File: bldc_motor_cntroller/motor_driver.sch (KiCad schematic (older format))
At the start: 70 parts, among them J10 MR30PW-M 15A (30A), Q3 CSD18540Q5B, Q4 CSD18540Q5B, Q5 CSD18540Q5B, Q6 CSD18540Q5B, Q7 CSD18540Q5B, Q8 CSD18540Q5B, U4 DRV8301DCAR

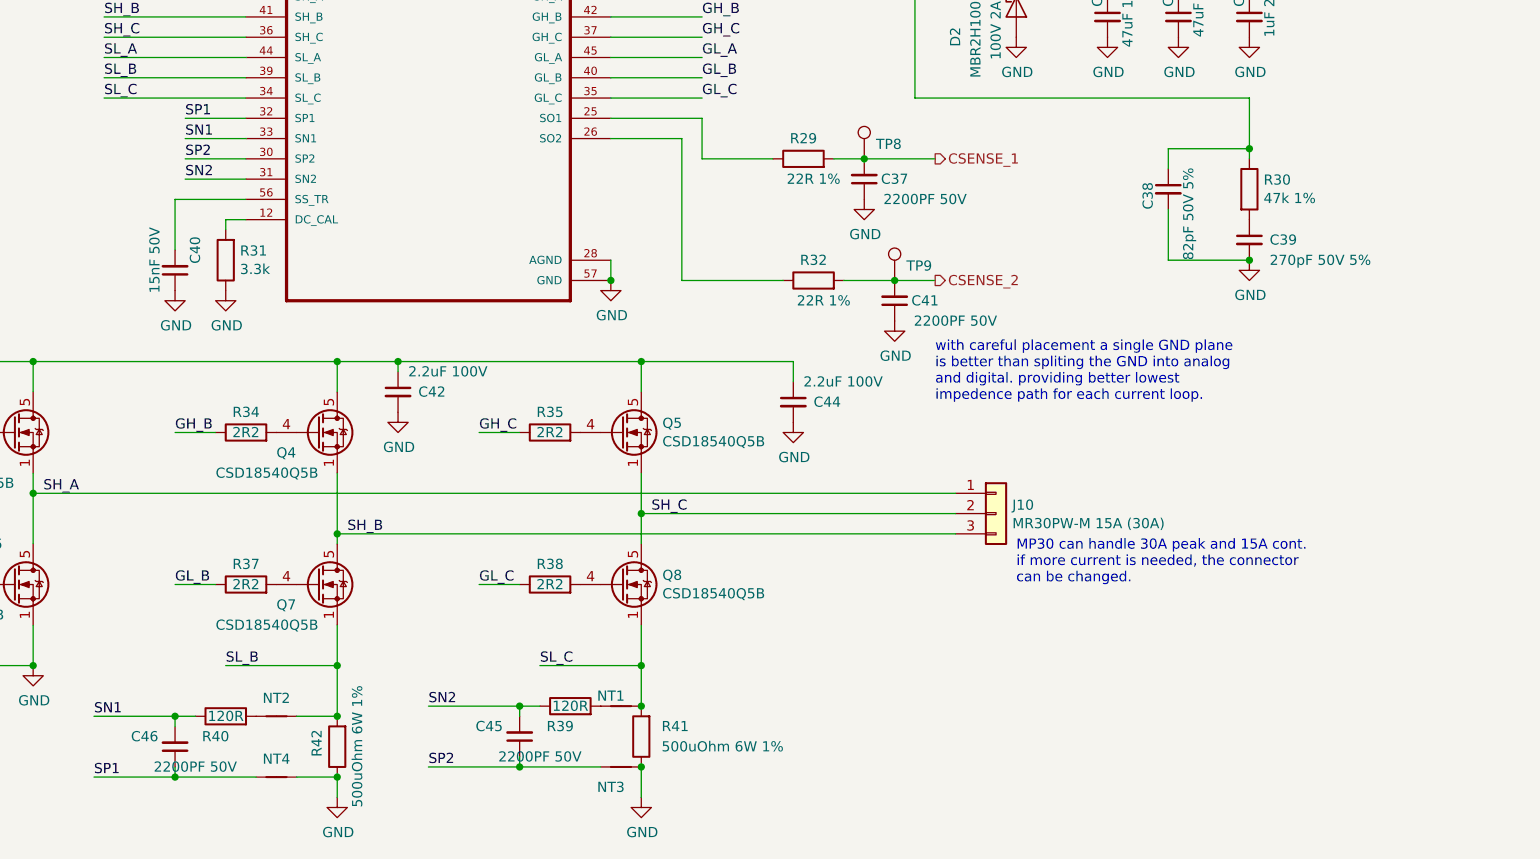
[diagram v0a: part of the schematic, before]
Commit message: improved assembly documentation
Signed-off-by: azmat bilal <azmat.bilal@outlook.com>
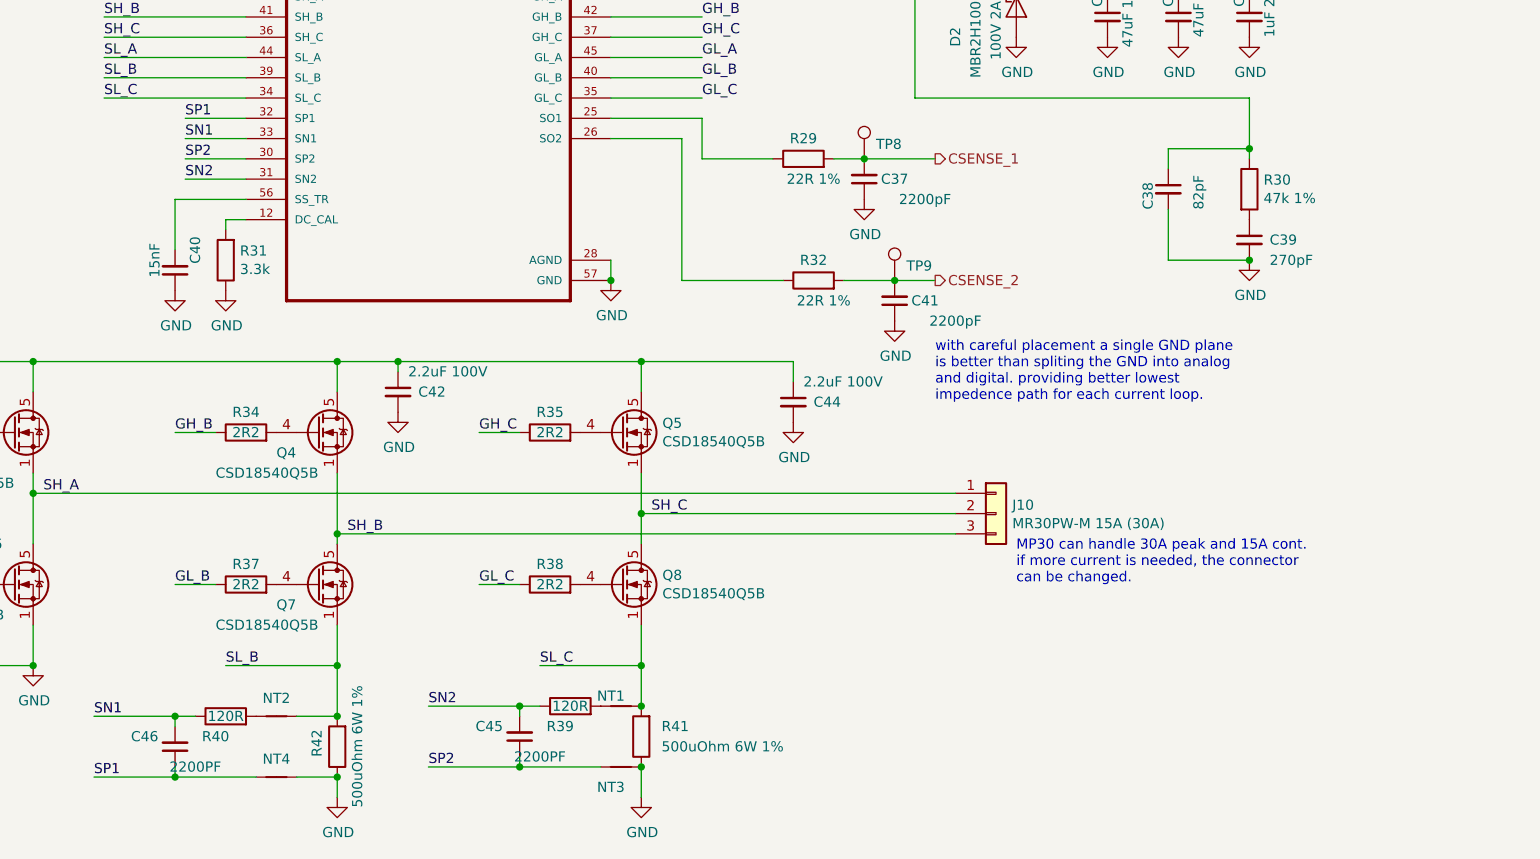
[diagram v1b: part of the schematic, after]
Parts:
- C37, C41: value 2200PF 50V -> 2200pF
- C38: value 82pF 50V 5% -> 82pF
- C39: value 270pF 50V 5% -> 270pF
- C40: value 15nF 50V -> 15nF
- C45, C46: value 2200PF 50V -> 2200PF
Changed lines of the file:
@@
 P 8100 4500
 F 0 "C38" V 8000 4400 50  0000 L CNN
-F 1 "82pF 50V 5%" V 8200 4150 50  0000 L CNN
+F 1 "82pF" V 8250 4400 50  0000 L CNN
 F 2 "Capacitor_SMD:C_0402_1005Metric" H 8100 4500 50  0001 C CNN
 F 3 "~" H 8100 4500 50  0001 C CNN
@@
 P 8500 4750
 F 0 "C39" H 8600 4750 50  0000 L CNN
-F 1 "270pF 50V 5%" H 8600 4650 50  0000 L CNN
+F 1 "270pF" H 8600 4650 50  0000 L CNN
 F 2 "Capacitor_SMD:C_0402_1005Metric" H 8500 4750 50  0001 C CNN
 F 3 "~" H 8500 4750 50  0001 C CNN
@@
 P 3200 7250
 F 0 "C46" H 3350 7200 50  0000 C CNN
-F 1 "2200PF 50V" H 3100 7350 50  0000 C CNN
+F 1 "2200PF" H 3100 7350 50  0000 C CNN
 F 2 "Capacitor_SMD:C_0402_1005Metric" H 3200 7250 50  0001 C CNN
 F 3 "~" H 3200 7250 50  0001 C CNN
@@
 P 4900 7200
 F 0 "C45" H 5050 7150 50  0000 C CNN
-F 1 "2200PF 50V" H 4800 7300 50  0000 C CNN
+F 1 "2200PF" H 4800 7300 50  0000 C CNN
 F 2 "Capacitor_SMD:C_0402_1005Metric" H 4900 7200 50  0001 C CNN
 F 3 "~" H 4900 7200 50  0001 C CNN
@@
 P 3200 4900
 F 0 "C40" V 3100 4800 50  0000 C CNN
-F 1 "15nF 50V" V 3300 4850 50  0000 C CNN
+F 1 "15nF" V 3300 4850 50  0000 C CNN
 F 2 "Capacitor_SMD:C_0402_1005Metric" H 3200 4900 50  0001 C CNN
 F 3 "~" H 3200 4900 50  0001 C CNN
@@
 P 6750 5050
 F 0 "C41" H 6600 5050 50  0000 C CNN
-F 1 "2200PF 50V" H 6450 5150 50  0000 C CNN
+F 1 "2200pF" H 6450 5150 50  0000 C CNN
 F 2 "Capacitor_SMD:C_0402_1005Metric" H 6750 5050 50  0001 C CNN
 F 3 "~" H 6750 5050 50  0001 C CNN
@@
 P 6600 4450
 F 0 "C37" H 6450 4450 50  0000 C CNN
-F 1 "2200PF 50V" H 6300 4550 50  0000 C CNN
+F 1 "2200pF" H 6300 4550 50  0000 C CNN
 F 2 "Capacitor_SMD:C_0402_1005Metric" H 6600 4450 50  0001 C CNN
 F 3 "~" H 6600 4450 50  0001 C CNN

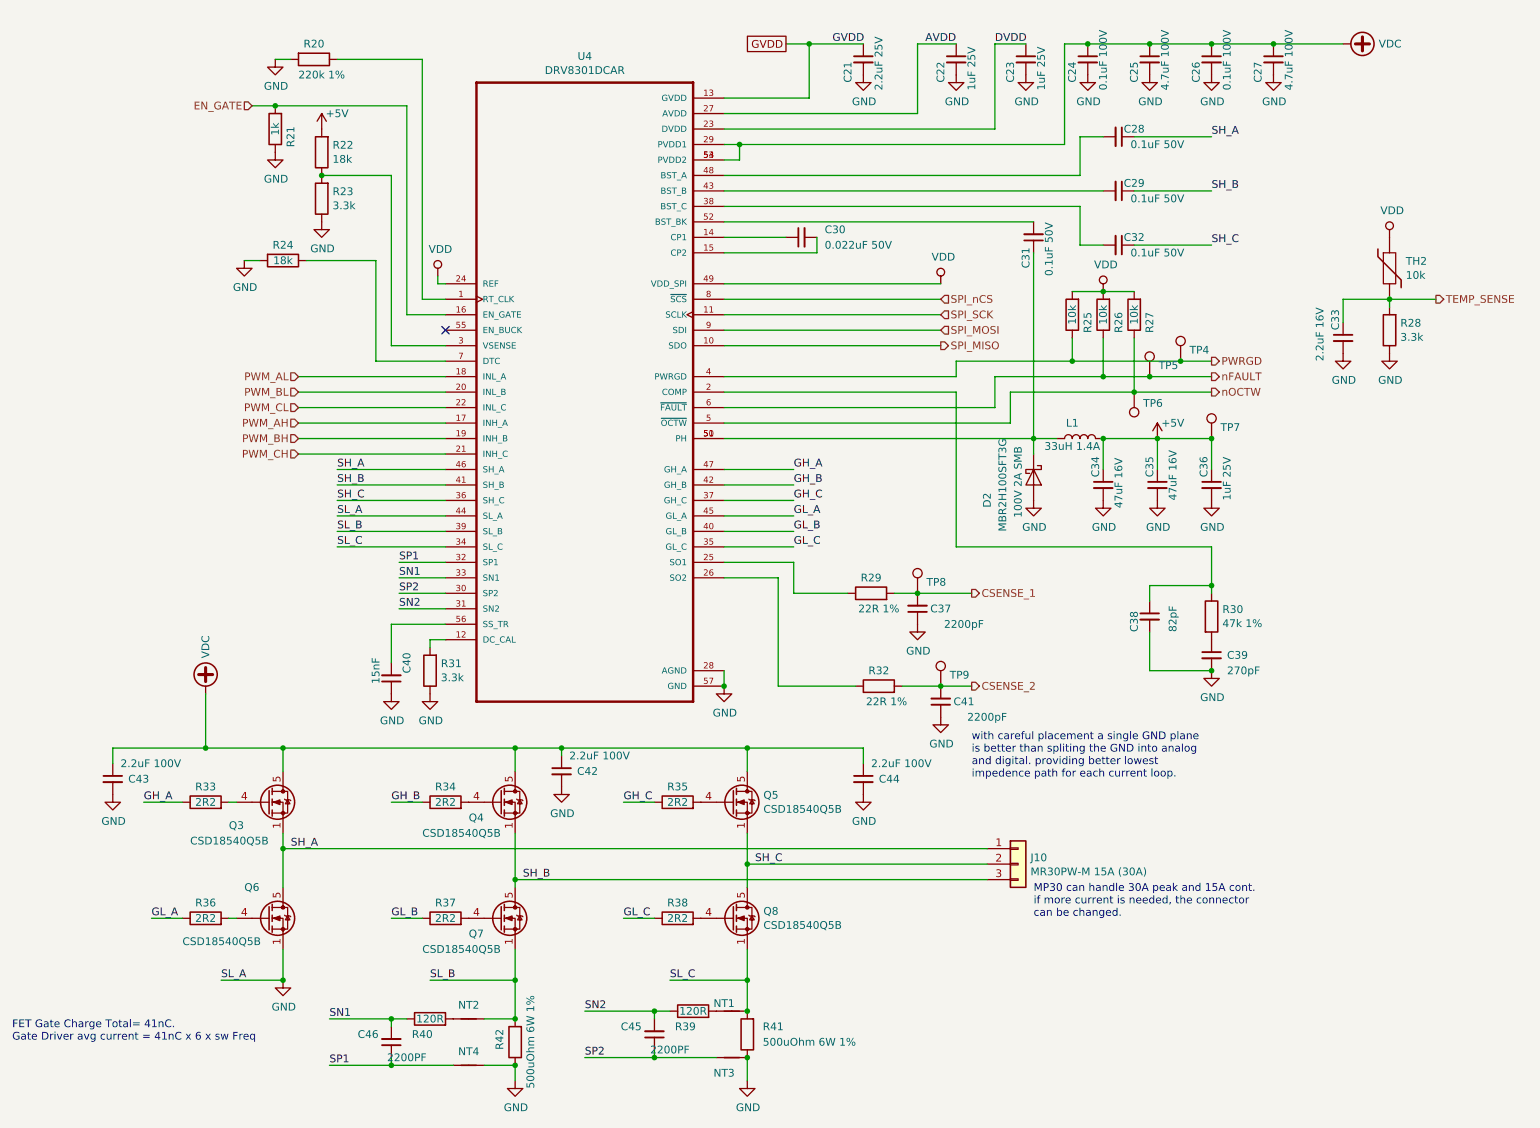
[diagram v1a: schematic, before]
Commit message: improved BOM
Signed-off-by: azmat bilal <azmat.bilal@outlook.com>
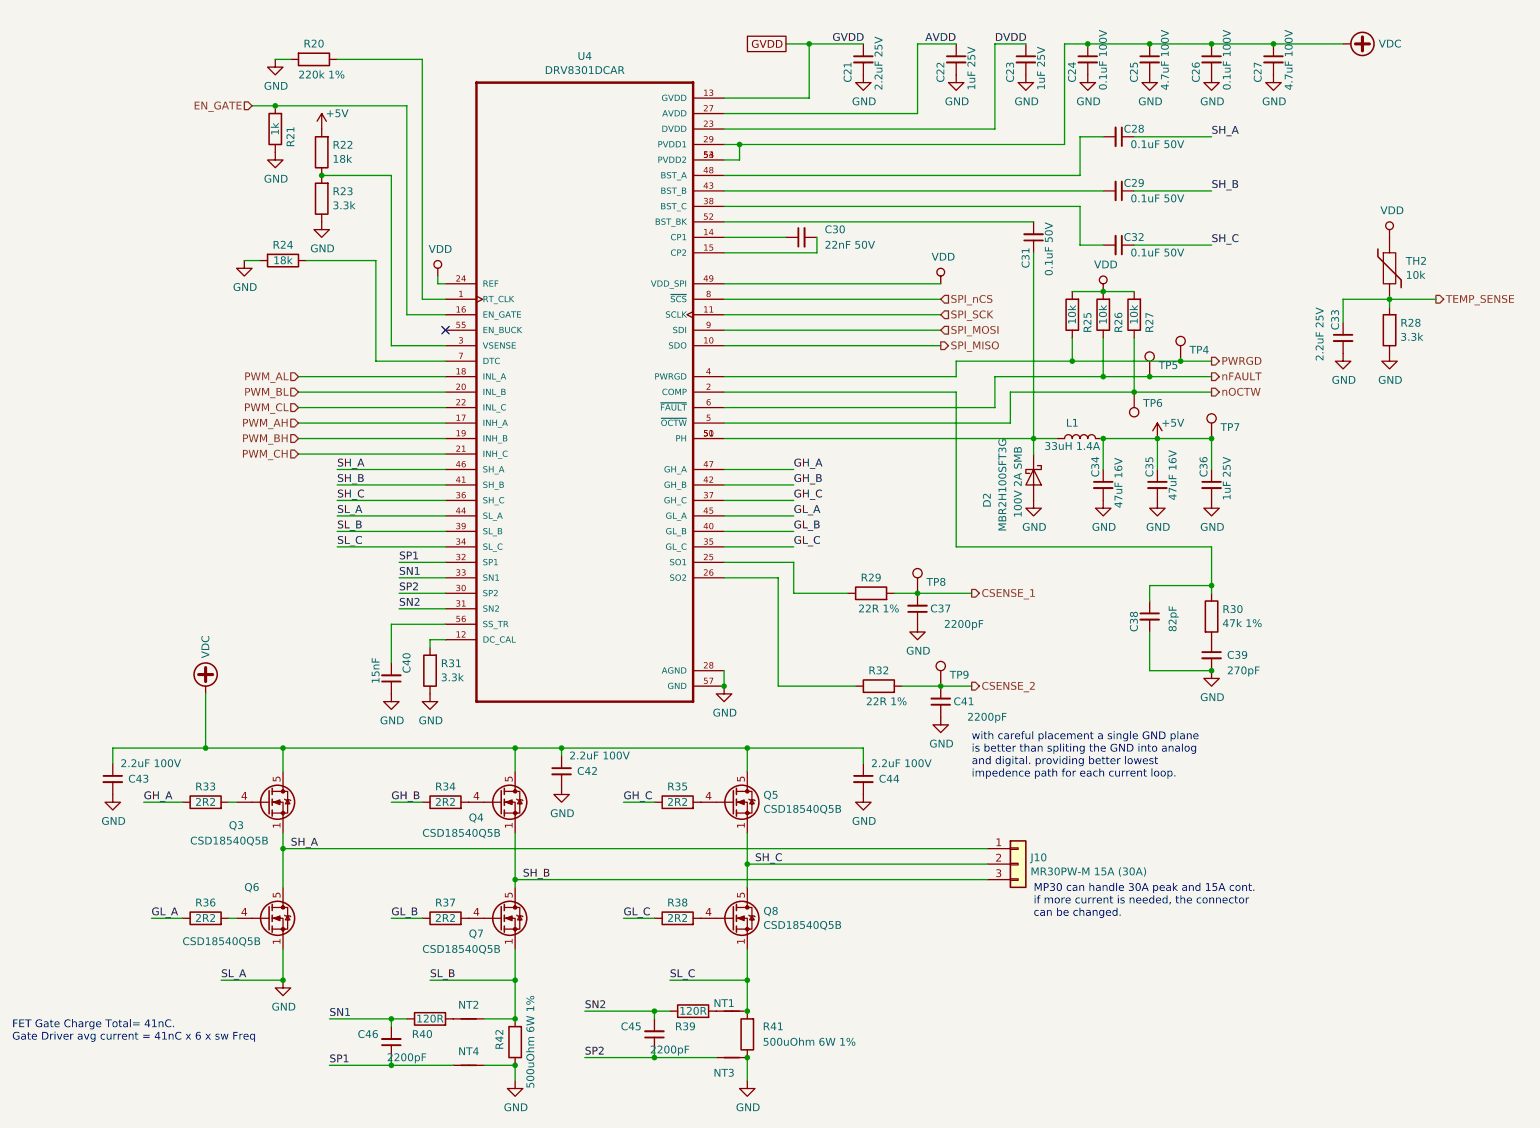
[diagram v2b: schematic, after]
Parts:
- C21: MPN (none) -> GRM155C81E225KE11D
- C22, C23, C36: MPN (none) -> GMK105CC6105MV-F
- C24, C26: MPN (none) -> GRM155R62A104KE14D
- C25, C27: MPN (none) -> HMK325C7475KN-TE
- C28, C29, C31, C32: MPN (none) -> GCM155L8EH104KE07D
- C30: value 0.022uF 50V -> 22nF 50V; MPN (none) -> C0402C223K5REC7411
- C33: value 2.2uF 16V -> 2.2uF 25V; MPN (none) -> GRM155C81E225KE11D
- C34, C35: MPN (none) -> GRM32EC81C476KE15L
- C37, C41: MPN (none) -> C0402C222J3GEC7411
- C38: MPN (none) -> VJ0402A820JXACW1BC
- C39: MPN (none) -> GRM1555C1H271FA01D
- C40: MPN (none) -> GCM155R71E153JA55D
- C42, C43, C44: MPN (none) -> C1210C225K1RACAUTO
- C45, C46: value 2200PF -> 2200pF; MPN (none) -> C0402C222J3GEC7411
- J10, NT1, NT2, NT3, NT4, TP4, TP5, TP6, TP7, TP8, TP9: MPN (none) -> -
- Q3, Q4, Q5, Q6, Q7, Q8: MPN (none) -> CSD18540Q5BT
- R20: MPN (none) -> CRCW0402220KFKEDC
- R21: MPN (none) -> ERJ-2RKF1001X
- R22, R24: MPN (none) -> CRCW040218K0FKED
- R23, R28, R31: MPN (none) -> CRCW04023K30FKEDC
- R25, R26, R27, TH2: MPN (none) -> CRCW040210K0FKEDC
- R29, R32: MPN (none) -> CRCW040222R0FKEDC
- R30: MPN (none) -> CRGP0402F47K
- R33, R34, R35, R36, R37, R38: MPN (none) -> CRCW04022R20FKEDC
- R39, R40: MPN (none) -> ERJ-2RKF1200X
- R41, R42: MPN (none) -> CSS2H-2512R-L500F
- U4: Field6 5591 -> (none); MPN (none) -> DRV8301DCAR
